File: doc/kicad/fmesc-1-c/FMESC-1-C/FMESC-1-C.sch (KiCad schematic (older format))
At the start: 22 parts, among them J1 Conn_01x02, J2 Conn_01x02, J3 Conn_01x02, J4 Conn_01x02, J5 Conn_01x02, J6 Conn_01x02, U1 FD6288Q

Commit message: doc/kicad: FMESC-1-C add PCB
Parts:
- J1, J2, J3, J4, J5, J6, JP1: footprint (none) -> fmlibf:JT_2P_1.0mm
- JC1: footprint (none) -> fmlibf:JS_12P_1.0mm
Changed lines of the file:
@@
 AR Path="/5FA3EBFA/5FAA6E02" Ref="#PWR?"  Part="1"
 AR Path="/5FA3F05C/5FAA6E02" Ref="#PWR?"  Part="1"
-F 0 "#PWR?" H 4500 2550 50  0001 C CNN
+AR Path="/5FAA6E02" Ref="#PWR0103"  Part="1"
+F 0 "#PWR0103" H 4500 2550 50  0001 C CNN
 F 1 "GND" H 4505 2627 50  0000 C CNN
 F 2 "" H 4500 2800 50  0001 C CNN
@@
 F 0 "J1" H 1418 3225 50  0000 C CNN
 F 1 "Conn_01x02" H 1418 3316 50  0000 C CNN
-F 2 "" H 1500 3550 50  0001 C CNN
+F 2 "fmlibf:JT_2P_1.0mm" H 1500 3550 50  0001 C CNN
 F 3 "~" H 1500 3550 50  0001 C CNN
 	1    1500 3550
@@
 F 0 "J2" H 1418 3725 50  0000 C CNN
 F 1 "Conn_01x02" H 1418 3816 50  0000 C CNN
-F 2 "" H 1500 4050 50  0001 C CNN
+F 2 "fmlibf:JT_2P_1.0mm" H 1500 4050 50  0001 C CNN
 F 3 "~" H 1500 4050 50  0001 C CNN
 	1    1500 4050
@@
 F 0 "J3" H 1418 4225 50  0000 C CNN
 F 1 "Conn_01x02" H 1418 4316 50  0000 C CNN
-F 2 "" H 1500 4550 50  0001 C CNN
+F 2 "fmlibf:JT_2P_1.0mm" H 1500 4550 50  0001 C CNN
 F 3 "~" H 1500 4550 50  0001 C CNN
 	1    1500 4550
@@
 F 0 "J4" H 1418 4725 50  0000 C CNN
 F 1 "Conn_01x02" H 1418 4816 50  0000 C CNN
-F 2 "" H 1500 5050 50  0001 C CNN
+F 2 "fmlibf:JT_2P_1.0mm" H 1500 5050 50  0001 C CNN
 F 3 "~" H 1500 5050 50  0001 C CNN
 	1    1500 5050
@@
 F 0 "J5" H 1418 5225 50  0000 C CNN
 F 1 "Conn_01x02" H 1418 5316 50  0000 C CNN
-F 2 "" H 1500 5550 50  0001 C CNN
+F 2 "fmlibf:JT_2P_1.0mm" H 1500 5550 50  0001 C CNN
 F 3 "~" H 1500 5550 50  0001 C CNN
 	1    1500 5550
@@
 F 0 "J6" H 1418 5725 50  0000 C CNN
 F 1 "Conn_01x02" H 1418 5816 50  0000 C CNN
-F 2 "" H 1500 6050 50  0001 C CNN
+F 2 "fmlibf:JT_2P_1.0mm" H 1500 6050 50  0001 C CNN
 F 3 "~" H 1500 6050 50  0001 C CNN
 	1    1500 6050
@@
 F 0 "JP1" H 1418 2725 50  0000 C CNN
 F 1 "Conn_01x02" H 1418 2816 50  0000 C CNN
-F 2 "" H 1500 3050 50  0001 C CNN
+F 2 "fmlibf:JT_2P_1.0mm" H 1500 3050 50  0001 C CNN
 F 3 "~" H 1500 3050 50  0001 C CNN
 	1    1500 3050
@@
 F 0 "JC1" H 2918 2717 50  0000 C CNN
 F 1 "Conn_01x12" H 2918 2626 50  0000 C CNN
-F 2 "" H 3000 2000 50  0001 C CNN
+F 2 "fmlibf:JS_12P_1.0mm" H 3000 2000 50  0001 C CNN
 F 3 "~" H 3000 2000 50  0001 C CNN
 	1    3000 2000

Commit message: doc/kicad: FMESC-1-C PCB layout
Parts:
- removed JC1: Conn_01x12, fmlibf:JS_12P_1.0mm, symbol Connector_Generic:Conn_01x12
- added JC1, JC2, JC3: Conn_01x04, fmlibf:JS_4P_1.0mm, symbol Connector_Generic:Conn_01x04
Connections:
- net A1: now also JC3.2 (Pin_2)
- net B1: now also JC3.3 (Pin_3)
- net C1: now also JC3.4 (Pin_4)
- net CAH1: now also JC2.2 (Pin_2)
- net CAL1: now also JC1.2 (Pin_2)
- net CBH1: now also JC2.3 (Pin_3)
- net CBL1: now also JC1.3 (Pin_3)
- net CCH1: now also JC2.4 (Pin_4)
- net CCL1: now also JC1.4 (Pin_4)
- net GND: now also JC1.1 (Pin_1), JC2.1 (Pin_1), JC3.1 (Pin_1)
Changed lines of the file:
@@
 Wire Wire Line
 	1700 5950 1850 5950
-$Comp
-L Connector_Generic:Conn_01x12 JC1
-U 1 1 5FAB3375
-P 3000 2000
-F 0 "JC1" H 2918 2717 50  0000 C CNN
-F 1 "Conn_01x12" H 2918 2626 50  0000 C CNN
-F 2 "fmlibf:JS_12P_1.0mm" H 3000 2000 50  0001 C CNN
-F 3 "~" H 3000 2000 50  0001 C CNN
-	1    3000 2000
-	-1   0    0    -1
-$EndComp
 Text Label 4850 2200 2    50   ~ 0
 CAL1
@@
 Text Label 5250 1800 1    50   ~ 0
 CCH1
-Text Label 3200 1500 0    50   ~ 0
+$Comp
+L Connector_Generic:Conn_01x04 JC1
+U 1 1 5FA7FB06
+P 8500 2100
+F 0 "JC1" H 8580 2092 50  0000 L CNN
+F 1 "Conn_01x04" H 8580 2001 50  0000 L CNN
+F 2 "fmlibf:JS_4P_1.0mm" H 8500 2100 50  0001 C CNN
+F 3 "~" H 8500 2100 50  0001 C CNN
+	1    8500 2100
+	1    0    0    -1
+$EndComp
+$Comp
+L Connector_Generic:Conn_01x04 JC2
+U 1 1 5FA7FF72
+P 8500 2600
+F 0 "JC2" H 8580 2592 50  0000 L CNN
+F 1 "Conn_01x04" H 8580 2501 50  0000 L CNN
+F 2 "fmlibf:JS_4P_1.0mm" H 8500 2600 50  0001 C CNN
+F 3 "~" H 8500 2600 50  0001 C CNN
+	1    8500 2600
+	1    0    0    -1
+$EndComp
+$Comp
+L Connector_Generic:Conn_01x04 JC3
+U 1 1 5FA80650
+P 8500 3100
+F 0 "JC3" H 8580 3092 50  0000 L CNN
+F 1 "Conn_01x04" H 8580 3001 50  0000 L CNN
+F 2 "fmlibf:JS_4P_1.0mm" H 8500 3100 50  0001 C CNN
+F 3 "~" H 8500 3100 50  0001 C CNN
+	1    8500 3100
+	1    0    0    -1
+$EndComp
+Text Label 8300 2000 2    50   ~ 0
+GND
+Text Label 8300 2500 2    50   ~ 0
+GND
+Text Label 8300 3000 2    50   ~ 0
+GND
+Text Label 8300 2100 2    50   ~ 0
 CAL1
-Text Label 3200 1600 0    50   ~ 0
+Text Label 8300 2200 2    50   ~ 0
 CBL1
-Text Label 3200 1700 0    50   ~ 0
+Text Label 8300 2300 2    50   ~ 0
 CCL1
-Text Label 3200 1800 0    50   ~ 0
+Text Label 8300 2600 2    50   ~ 0
 CAH1
-Text Label 3200 1900 0    50   ~ 0
+Text Label 8300 2700 2    50   ~ 0
 CBH1
-Text Label 3200 2000 0    50   ~ 0
+Text Label 8300 2800 2    50   ~ 0
 CCH1
-Text Label 3200 2100 0    50   ~ 0
-GND
-Text Label 3200 2200 0    50   ~ 0
+Text Label 8300 3100 2    50   ~ 0
 A1
-Text Label 3200 2300 0    50   ~ 0
+Text Label 8300 3200 2    50   ~ 0
 B1
-Text Label 3200 2400 0    50   ~ 0
+Text Label 8300 3300 2    50   ~ 0
 C1
-Text Label 3200 2500 0    50   ~ 0
-GND
-Text Label 3200 2600 0    50   ~ 0
-VC
 $EndSCHEMATC

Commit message: doc/kicad: FMESC-1-C PCB v0.1
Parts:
- D1, D2, D3: footprint Diode_SMD:D_SMA -> Diode_SMD:D_0603_1608Metric
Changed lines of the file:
@@
 Sheet 1 1
 Title "FMESC-1-C"
-Date "2020-11-08"
-Rev "TODO"
+Date "2020-11-09"
+Rev "v0.1"
 Comp "sceext"
 Comment1 ""
@@
 F 0 "D1" V 6546 1070 50  0000 R CNN
 F 1 "D" V 6455 1070 50  0000 R CNN
-F 2 "Diode_SMD:D_SMA" H 6500 1150 50  0001 C CNN
+F 2 "Diode_SMD:D_0603_1608Metric" H 6500 1150 50  0001 C CNN
 F 3 "~" H 6500 1150 50  0001 C CNN
 	1    6500 1150
@@
 F 0 "D2" V 7046 1070 50  0000 R CNN
 F 1 "D" V 6955 1070 50  0000 R CNN
-F 2 "Diode_SMD:D_SMA" H 7000 1150 50  0001 C CNN
+F 2 "Diode_SMD:D_0603_1608Metric" H 7000 1150 50  0001 C CNN
 F 3 "~" H 7000 1150 50  0001 C CNN
 	1    7000 1150
@@
 F 0 "D3" V 7546 1070 50  0000 R CNN
 F 1 "D" V 7455 1070 50  0000 R CNN
-F 2 "Diode_SMD:D_SMA" H 7500 1150 50  0001 C CNN
+F 2 "Diode_SMD:D_0603_1608Metric" H 7500 1150 50  0001 C CNN
 F 3 "~" H 7500 1150 50  0001 C CNN
 	1    7500 1150

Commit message: doc/kicad: FMESC-1-C update sch and clean
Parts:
- added R11, R13, R15, R21, R22, R23: 2k, Resistor_SMD:R_0402_1005Metric, symbol Device:R
- added R12, R14, R16: 20k, Resistor_SMD:R_0402_1005Metric, symbol Device:R
- J1, J2, J3, J4, J5, J6: footprint fmlibf:JT_2P_1.0mm -> fmlibf:JS_2P_1.0mm_2
- U1: footprint Package_DFN_QFN:QFN-24-1EP_4x4mm_P0.5mm_EP2.7x2.7mm -> fmlibf:QFN-24-1EP_4x4mm_P0.5mm_EP2.7x2.7mm_nopad
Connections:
- net A1: now also R12.2; no longer JC3.2 (Pin_2)
- net B1: now also R14.2; no longer JC3.3 (Pin_3)
- net C1: now also R16.2; no longer JC3.4 (Pin_4)
- net GND: now also R11.1, R13.1, R15.1; no longer JC3.1 (Pin_1)
- new net S0: JC3.1 (Pin_1), R21.1, R22.1, R23.1
- new net SA: JC3.2 (Pin_2), R11.2, R12.1, R21.2
- new net SB: JC3.3 (Pin_3), R13.2, R14.1, R22.2
- new net SC: JC3.4 (Pin_4), R15.2, R16.1, R23.2
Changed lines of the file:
@@
 Sheet 1 1
 Title "FMESC-1-C"
-Date "2020-11-09"
-Rev "v0.1"
+Date "2020-11-15"
+Rev "v0.2"
 Comp "sceext"
 Comment1 ""
@@
 F 0 "U1" H 5450 2500 50  0000 L CNN
 F 1 "FD6288Q" H 5350 2250 50  0000 L CNN
-F 2 "Package_DFN_QFN:QFN-24-1EP_4x4mm_P0.5mm_EP2.7x2.7mm" H 5500 1600 50  0001 C CNN
+F 2 "fmlibf:QFN-24-1EP_4x4mm_P0.5mm_EP2.7x2.7mm_nopad" H 5500 1600 50  0001 C CNN
 F 3 "" H 4950 2700 50  0001 C CNN
 	1    5500 2450
@@
 F 0 "J1" H 1418 3225 50  0000 C CNN
 F 1 "Conn_01x02" H 1418 3316 50  0000 C CNN
-F 2 "fmlibf:JT_2P_1.0mm" H 1500 3550 50  0001 C CNN
+F 2 "fmlibf:JS_2P_1.0mm_2" H 1500 3550 50  0001 C CNN
 F 3 "~" H 1500 3550 50  0001 C CNN
 	1    1500 3550
@@
 F 0 "J2" H 1418 3725 50  0000 C CNN
 F 1 "Conn_01x02" H 1418 3816 50  0000 C CNN
-F 2 "fmlibf:JT_2P_1.0mm" H 1500 4050 50  0001 C CNN
+F 2 "fmlibf:JS_2P_1.0mm_2" H 1500 4050 50  0001 C CNN
 F 3 "~" H 1500 4050 50  0001 C CNN
 	1    1500 4050
@@
 F 0 "J3" H 1418 4225 50  0000 C CNN
 F 1 "Conn_01x02" H 1418 4316 50  0000 C CNN
-F 2 "fmlibf:JT_2P_1.0mm" H 1500 4550 50  0001 C CNN
+F 2 "fmlibf:JS_2P_1.0mm_2" H 1500 4550 50  0001 C CNN
 F 3 "~" H 1500 4550 50  0001 C CNN
 	1    1500 4550
@@
 F 0 "J4" H 1418 4725 50  0000 C CNN
 F 1 "Conn_01x02" H 1418 4816 50  0000 C CNN
-F 2 "fmlibf:JT_2P_1.0mm" H 1500 5050 50  0001 C CNN
+F 2 "fmlibf:JS_2P_1.0mm_2" H 1500 5050 50  0001 C CNN
 F 3 "~" H 1500 5050 50  0001 C CNN
 	1    1500 5050
@@
 F 0 "J5" H 1418 5225 50  0000 C CNN
 F 1 "Conn_01x02" H 1418 5316 50  0000 C CNN
-F 2 "fmlibf:JT_2P_1.0mm" H 1500 5550 50  0001 C CNN
+F 2 "fmlibf:JS_2P_1.0mm_2" H 1500 5550 50  0001 C CNN
 F 3 "~" H 1500 5550 50  0001 C CNN
 	1    1500 5550
@@
 F 0 "J6" H 1418 5725 50  0000 C CNN
 F 1 "Conn_01x02" H 1418 5816 50  0000 C CNN
-F 2 "fmlibf:JT_2P_1.0mm" H 1500 6050 50  0001 C CNN
+F 2 "fmlibf:JS_2P_1.0mm_2" H 1500 6050 50  0001 C CNN
 F 3 "~" H 1500 6050 50  0001 C CNN
 	1    1500 6050
@@
 Text Label 8300 2500 2    50   ~ 0
 GND
-Text Label 8300 3000 2    50   ~ 0
-GND
 Text Label 8300 2100 2    50   ~ 0
 CAL1
@@
 Text Label 8300 2800 2    50   ~ 0
 CCH1
+$Comp
+L Device:R R?
+U 1 1 5FB18250
+P 7150 4000
+AR Path="/5FA1845D/5FB18250" Ref="R?"  Part="1"
+AR Path="/5FA433EC/5FB18250" Ref="R?"  Part="1"
+AR Path="/5FA435C0/5FB18250" Ref="R?"  Part="1"
+AR Path="/5FA4361C/5FB18250" Ref="R?"  Part="1"
+AR Path="/5FA3E74F/5FB18250" Ref="R?"  Part="1"
+AR Path="/5FA3EBFA/5FB18250" Ref="R?"  Part="1"
+AR Path="/5FA3F05C/5FB18250" Ref="R?"  Part="1"
+AR Path="/5FB18250" Ref="R12"  Part="1"
+F 0 "R12" V 6943 4000 50  0000 C CNN
+F 1 "20k" V 7034 4000 50  0000 C CNN
+F 2 "Resistor_SMD:R_0402_1005Metric" V 7080 4000 50  0001 C CNN
+F 3 "~" H 7150 4000 50  0001 C CNN
+	1    7150 4000
+	0    1    1    0
+$EndComp
+$Comp
+L Device:R R?
+U 1 1 5FB18793
+P 7150 4500
+AR Path="/5FA1845D/5FB18793" Ref="R?"  Part="1"
+AR Path="/5FA433EC/5FB18793" Ref="R?"  Part="1"
+AR Path="/5FA435C0/5FB18793" Ref="R?"  Part="1"
+AR Path="/5FA4361C/5FB18793" Ref="R?"  Part="1"
+AR Path="/5FA3E74F/5FB18793" Ref="R?"  Part="1"
+AR Path="/5FA3EBFA/5FB18793" Ref="R?"  Part="1"
+AR Path="/5FA3F05C/5FB18793" Ref="R?"  Part="1"
+AR Path="/5FB18793" Ref="R14"  Part="1"
+F 0 "R14" V 6943 4500 50  0000 C CNN
+F 1 "20k" V 7034 4500 50  0000 C CNN
+F 2 "Resistor_SMD:R_0402_1005Metric" V 7080 4500 50  0001 C CNN
+F 3 "~" H 7150 4500 50  0001 C CNN
+	1    7150 4500
+	0    1    1    0
+$EndComp
+$Comp
+L Device:R R?
+U 1 1 5FB18A77
+P 7150 5000
+AR Path="/5FA1845D/5FB18A77" Ref="R?"  Part="1"
+AR Path="/5FA433EC/5FB18A77" Ref="R?"  Part="1"
+AR Path="/5FA435C0/5FB18A77" Ref="R?"  Part="1"
+AR Path="/5FA4361C/5FB18A77" Ref="R?"  Part="1"
+AR Path="/5FA3E74F/5FB18A77" Ref="R?"  Part="1"
+AR Path="/5FA3EBFA/5FB18A77" Ref="R?"  Part="1"
+AR Path="/5FA3F05C/5FB18A77" Ref="R?"  Part="1"
+AR Path="/5FB18A77" Ref="R16"  Part="1"
+F 0 "R16" V 6943 5000 50  0000 C CNN
+F 1 "20k" V 7034 5000 50  0000 C CNN
+F 2 "Resistor_SMD:R_0402_1005Metric" V 7080 5000 50  0001 C CNN
+F 3 "~" H 7150 5000 50  0001 C CNN
+	1    7150 5000
+	0    1    1    0
+$EndComp
+$Comp
+L Device:R R?
+U 1 1 5FB18F67
+P 7850 4000
+AR Path="/5FA1845D/5FB18F67" Ref="R?"  Part="1"
+AR Path="/5FA433EC/5FB18F67" Ref="R?"  Part="1"
+AR Path="/5FA435C0/5FB18F67" Ref="R?"  Part="1"
+AR Path="/5FA4361C/5FB18F67" Ref="R?"  Part="1"
+AR Path="/5FA3E74F/5FB18F67" Ref="R?"  Part="1"
+AR Path="/5FA3EBFA/5FB18F67" Ref="R?"  Part="1"
+AR Path="/5FA3F05C/5FB18F67" Ref="R?"  Part="1"
+AR Path="/5FB18F67" Ref="R11"  Part="1"
+F 0 "R11" V 7643 4000 50  0000 C CNN
+F 1 "2k" V 7734 4000 50  0000 C CNN
+F 2 "Resistor_SMD:R_0402_1005Metric" V 7780 4000 50  0001 C CNN
+F 3 "~" H 7850 4000 50  0001 C CNN
+	1    7850 4000
+	0    1    1    0
+$EndComp
+$Comp
+L Device:R R?
+U 1 1 5FB19325
+P 7850 4500
+AR Path="/5FA1845D/5FB19325" Ref="R?"  Part="1"
+AR Path="/5FA433EC/5FB19325" Ref="R?"  Part="1"
+AR Path="/5FA435C0/5FB19325" Ref="R?"  Part="1"
+AR Path="/5FA4361C/5FB19325" Ref="R?"  Part="1"
+AR Path="/5FA3E74F/5FB19325" Ref="R?"  Part="1"
+AR Path="/5FA3EBFA/5FB19325" Ref="R?"  Part="1"
+AR Path="/5FA3F05C/5FB19325" Ref="R?"  Part="1"
+AR Path="/5FB19325" Ref="R13"  Part="1"
+F 0 "R13" V 7643 4500 50  0000 C CNN
+F 1 "2k" V 7734 4500 50  0000 C CNN
+F 2 "Resistor_SMD:R_0402_1005Metric" V 7780 4500 50  0001 C CNN
+F 3 "~" H 7850 4500 50  0001 C CNN
+	1    7850 4500
+	0    1    1    0
+$EndComp
+$Comp
+L Device:R R?
+U 1 1 5FB196E5
+P 7850 5000
+AR Path="/5FA1845D/5FB196E5" Ref="R?"  Part="1"
+AR Path="/5FA433EC/5FB196E5" Ref="R?"  Part="1"
+AR Path="/5FA435C0/5FB196E5" Ref="R?"  Part="1"
+AR Path="/5FA4361C/5FB196E5" Ref="R?"  Part="1"
+AR Path="/5FA3E74F/5FB196E5" Ref="R?"  Part="1"
+AR Path="/5FA3EBFA/5FB196E5" Ref="R?"  Part="1"
+AR Path="/5FA3F05C/5FB196E5" Ref="R?"  Part="1"
+AR Path="/5FB196E5" Ref="R15"  Part="1"
+F 0 "R15" V 7643 5000 50  0000 C CNN
+F 1 "2k" V 7734 5000 50  0000 C CNN
+F 2 "Resistor_SMD:R_0402_1005Metric" V 7780 5000 50  0001 C CNN
+F 3 "~" H 7850 5000 50  0001 C CNN
+	1    7850 5000
+	0    1    1    0
+$EndComp
+Wire Wire Line
+	7300 4000 7700 4000
+Wire Wire Line
+	7300 4500 7700 4500
+Wire Wire Line
+	7300 5000 7700 5000
+Wire Wire Line
+	8000 4000 8000 4500
+Connection ~ 8000 4500
+Wire Wire Line
+	8000 4500 8000 5000
+Text Label 8000 4500 0    50   ~ 0
+GND
+Text Label 7000 4000 2    50   ~ 0
+A1
+Text Label 7000 4500 2    50   ~ 0
+B1
+Text Label 7000 5000 2    50   ~ 0
+C1
+Text Label 7500 4000 0    50   ~ 0
+SA
+Text Label 7500 4500 0    50   ~ 0
+SB
+Text Label 7500 5000 0    50   ~ 0
+SC
+Text Label 8300 3000 2    50   ~ 0
+S0
 Text Label 8300 3100 2    50   ~ 0
-A1
+SA
 Text Label 8300 3200 2    50   ~ 0
-B1
+SB
 Text Label 8300 3300 2    50   ~ 0
-C1
+SC
+$Comp
+L Device:R R?
+U 1 1 5FB20F21
+P 8650 4000
+AR Path="/5FA1845D/5FB20F21" Ref="R?"  Part="1"
+AR Path="/5FA433EC/5FB20F21" Ref="R?"  Part="1"
+AR Path="/5FA435C0/5FB20F21" Ref="R?"  Part="1"
+AR Path="/5FA4361C/5FB20F21" Ref="R?"  Part="1"
+AR Path="/5FA3E74F/5FB20F21" Ref="R?"  Part="1"
+AR Path="/5FA3EBFA/5FB20F21" Ref="R?"  Part="1"
+AR Path="/5FA3F05C/5FB20F21" Ref="R?"  Part="1"
+AR Path="/5FB20F21" Ref="R21"  Part="1"
+F 0 "R21" V 8443 4000 50  0000 C CNN
+F 1 "2k" V 8534 4000 50  0000 C CNN
+F 2 "Resistor_SMD:R_0402_1005Metric" V 8580 4000 50  0001 C CNN
+F 3 "~" H 8650 4000 50  0001 C CNN
+	1    8650 4000
+	0    1    1    0
+$EndComp
+$Comp
+L Device:R R?
+U 1 1 5FB2128F
+P 8650 4500
+AR Path="/5FA1845D/5FB2128F" Ref="R?"  Part="1"
+AR Path="/5FA433EC/5FB2128F" Ref="R?"  Part="1"
+AR Path="/5FA435C0/5FB2128F" Ref="R?"  Part="1"
+AR Path="/5FA4361C/5FB2128F" Ref="R?"  Part="1"
+AR Path="/5FA3E74F/5FB2128F" Ref="R?"  Part="1"
+AR Path="/5FA3EBFA/5FB2128F" Ref="R?"  Part="1"
+AR Path="/5FA3F05C/5FB2128F" Ref="R?"  Part="1"
+AR Path="/5FB2128F" Ref="R22"  Part="1"
+F 0 "R22" V 8443 4500 50  0000 C CNN
+F 1 "2k" V 8534 4500 50  0000 C CNN
+F 2 "Resistor_SMD:R_0402_1005Metric" V 8580 4500 50  0001 C CNN
+F 3 "~" H 8650 4500 50  0001 C CNN
+	1    8650 4500
+	0    1    1    0
+$EndComp
+$Comp
+L Device:R R?
+U 1 1 5FB21566
+P 8650 5000
+AR Path="/5FA1845D/5FB21566" Ref="R?"  Part="1"
+AR Path="/5FA433EC/5FB21566" Ref="R?"  Part="1"
+AR Path="/5FA435C0/5FB21566" Ref="R?"  Part="1"
+AR Path="/5FA4361C/5FB21566" Ref="R?"  Part="1"
+AR Path="/5FA3E74F/5FB21566" Ref="R?"  Part="1"
+AR Path="/5FA3EBFA/5FB21566" Ref="R?"  Part="1"
+AR Path="/5FA3F05C/5FB21566" Ref="R?"  Part="1"
+AR Path="/5FB21566" Ref="R23"  Part="1"
+F 0 "R23" V 8443 5000 50  0000 C CNN
+F 1 "2k" V 8534 5000 50  0000 C CNN
+F 2 "Resistor_SMD:R_0402_1005Metric" V 8580 5000 50  0001 C CNN
+F 3 "~" H 8650 5000 50  0001 C CNN
+	1    8650 5000
+	0    1    1    0
+$EndComp
+Wire Wire Line
+	8800 4000 8800 4500
+Connection ~ 8800 4500
+Wire Wire Line
+	8800 4500 8800 5000
+Text Label 8800 4500 0    50   ~ 0
+S0
+Text Label 8500 4000 2    50   ~ 0
+SA
+Text Label 8500 4500 2    50   ~ 0
+SB
+Text Label 8500 5000 2    50   ~ 0
+SC
 $EndSCHEMATC

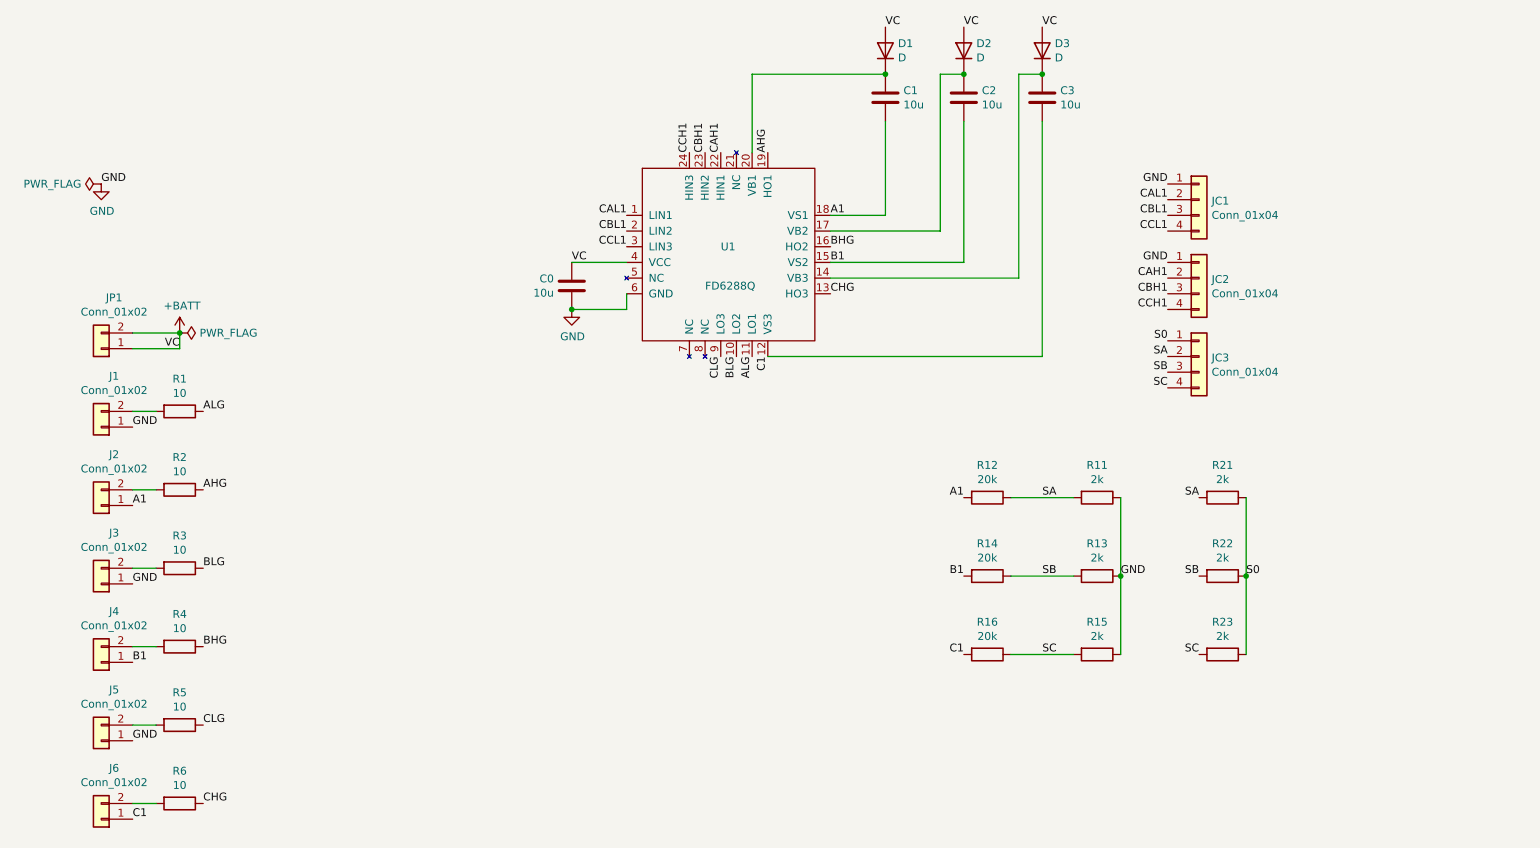
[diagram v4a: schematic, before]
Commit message: doc/kicad: FMESC-1-C PCB clean and use FMPCBVDL-1
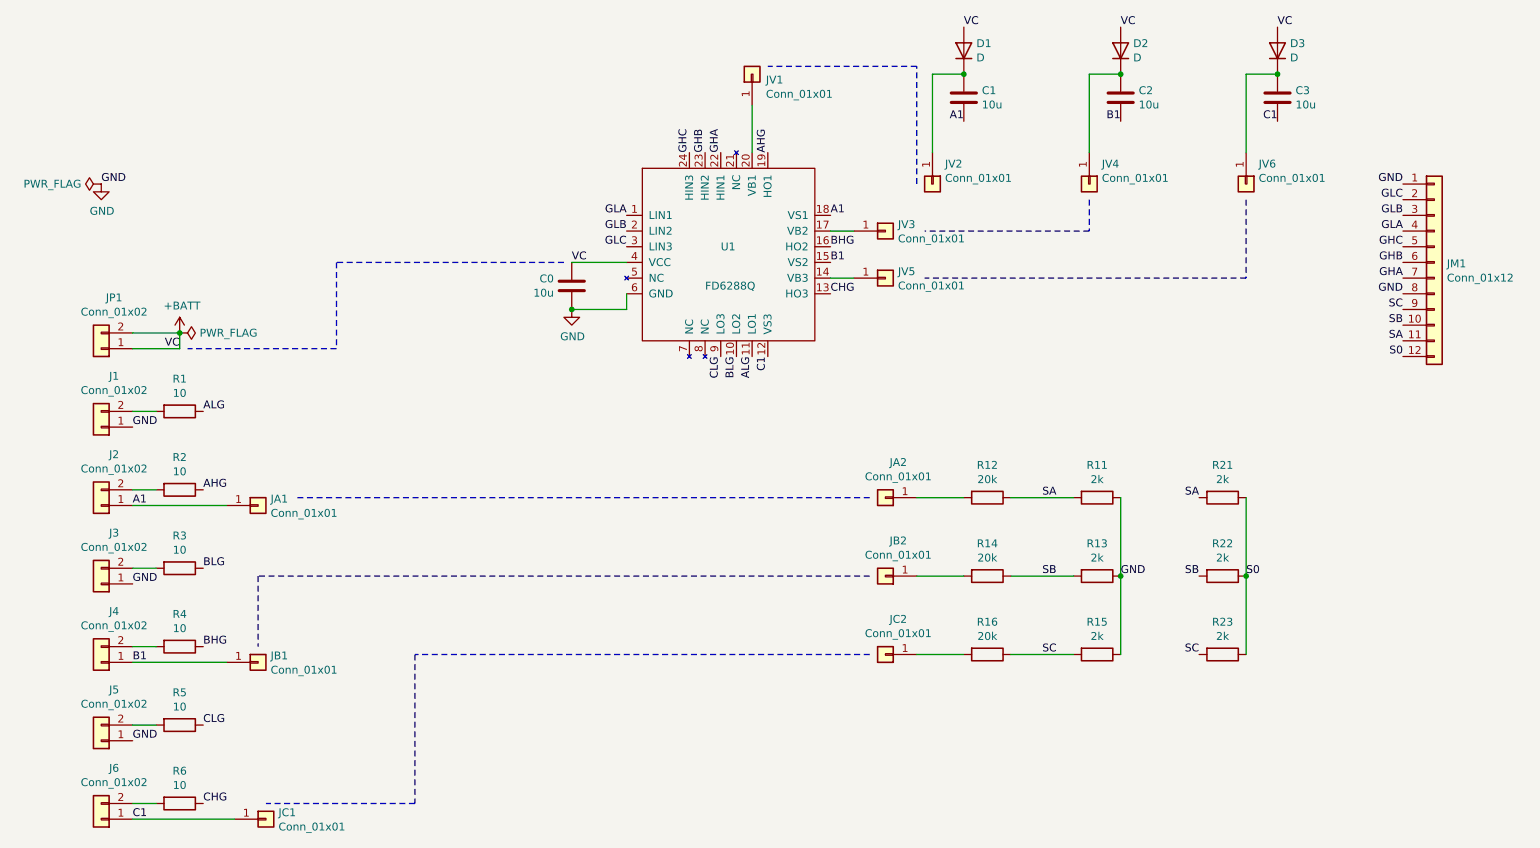
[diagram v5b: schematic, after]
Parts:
- removed JC1, JC2, JC3: Conn_01x04, fmlibf:JS_4P_1.0mm, symbol Connector_Generic:Conn_01x04
- added JA1, JA2, JB1, JB2, JC1, JC2, JV1, JV2, JV3, JV4, JV5, JV6: Conn_01x01, fmlibf:JS_1P_1x1mm, symbol Connector_Generic:Conn_01x01
- added JM1: Conn_01x12, fmlibf:JS_12P_1.0mm, symbol Connector_Generic:Conn_01x12
- J1, J2, J3, J4, J5, J6: footprint fmlibf:JS_2P_1.0mm_2 -> fmlibf:FMPCBVDL-1-S
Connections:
- net A1: now also JA1.1 (Pin_1); no longer R12.2
- net B1: now also JB1.1 (Pin_1); no longer R14.2
- net C1: now also JC1.1 (Pin_1); no longer R16.2
- net GND: now also JM1.1 (Pin_1), JM1.8 (Pin_8)
- net S0: now also JM1.12 (Pin_12)
- net SA: now also JM1.11 (Pin_11)
- net SB: now also JM1.10 (Pin_10)
- net SC: now also JM1.9 (Pin_9)
- net at C3.1, D3.1 (K): now also JV6.1 (Pin_1); no longer U1.14 (VB3)
- net at C2.1, D2.1 (K): now also JV4.1 (Pin_1); no longer U1.17 (VB2)
- net at C1.1, D1.1 (K): now also JV2.1 (Pin_1); no longer U1.20 (VB1)
- net CAH1 renamed GHA
- net GHA: now also JM1.7 (Pin_7)
- net CAL1 renamed GLA
- net GLA: now also JM1.4 (Pin_4)
- net CBH1 renamed GHB
- net GHB: now also JM1.6 (Pin_6)
- net CBL1 renamed GLB
- net GLB: now also JM1.3 (Pin_3)
- net CCH1 renamed GHC
- net GHC: now also JM1.5 (Pin_5)
- net CCL1 renamed GLC
- net GLC: now also JM1.2 (Pin_2)
- new net: JV5.1 (Pin_1), U1.14 (VB3)
- new net: JV3.1 (Pin_1), U1.17 (VB2)
- new net: JV1.1 (Pin_1), U1.20 (VB1)
- new net: JA2.1 (Pin_1), R12.2
- new net: JB2.1 (Pin_1), R14.2
- new net: JC2.1 (Pin_1), R16.2
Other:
- moved on the sheet: C1, C2, C3, D1, D2, D3
